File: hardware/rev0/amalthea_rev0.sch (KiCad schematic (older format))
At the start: 27 parts, among them J1 USB_B_Micro, J2 USB_B_Micro, J3 Conn_Coaxial, J4 Conn_Coaxial, J8 Conn_Coaxial, J9 Conn_Coaxial, SW1 BTN_RECOVERY, SW2 BTN_DFU, SW3 BTN_RESET, Y1 DSC60xx

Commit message: Pick part numbers for BOM
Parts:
- D1, D8: Manufacturer_Part_Number (none) -> PMEG3050EP,115
- D2: Manufacturer_Part_Number (none) -> KR DELMS1.22-RHSI-24-E6L6
- D3: Manufacturer_Part_Number (none) -> KO DELMS1.22-SGTH-24-E6L6
- D4: Manufacturer_Part_Number (none) -> KY DELMS1.22-RHSI-26-G6N4
- D5: Manufacturer_Part_Number (none) -> KG DELMS1.22-PHQI-24-E6L6
- D6: Manufacturer_Part_Number (none) -> KB DELPS2.12-QHRI-24-Z555-10-S
- J1, J2: Manufacturer_Part_Number (none) -> 10103594-0001LF
- J3, J4, J8, J9: Manufacturer_Part_Number (none) -> CONSMA003.062
- R26, R27, R28, R29, R30, R31: Manufacturer_Part_Number (none) -> CRCW0402330RFKEDC
- SW1, SW2, SW3: Manufacturer_Part_Number (none) -> FSMRA3JH
- Y1: Manufacturer_Part_Number (none) -> DSC6001MI2A-060.0000
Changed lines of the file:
@@
 F 2 "amalthea:SOD128" H 6300 4850 50  0001 C CNN
 F 3 "~" H 6300 4850 50  0001 C CNN
+F 4 "PMEG3050EP,115" H 6300 4850 50  0001 C CNN "Manufacturer_Part_Number"
 	1    6300 4850
 	1    0    0    -1
@@
 F 2 "Connector_USB:USB_Micro-B_Amphenol_10103594-0001LF_Horizontal" H 7250 5000 50  0001 C CNN
 F 3 "~" H 7250 5000 50  0001 C CNN
+F 4 "10103594-0001LF" H 7100 5050 50  0001 C CNN "Manufacturer_Part_Number"
 	1    7100 5050
 	-1   0    0    -1
@@
 F 2 "Connector_USB:USB_Micro-B_Amphenol_10103594-0001LF_Horizontal" H 1050 3850 50  0001 C CNN
 F 3 "~" H 1050 3850 50  0001 C CNN
+F 4 "10103594-0001LF" H 900 3900 50  0001 C CNN "Manufacturer_Part_Number"
 	1    900  3900
 	1    0    0    -1
@@
 F 2 "amalthea:SOD128" H 1350 3550 50  0001 C CNN
 F 3 "~" H 1350 3550 50  0001 C CNN
+F 4 "PMEG3050EP,115" H 1350 3550 50  0001 C CNN "Manufacturer_Part_Number"
 	1    1350 3550
 	-1   0    0    1
@@
 F 2 "Crystal:Crystal_SMD_2016-4Pin_2.0x1.6mm" H 1050 2400 50  0001 C CNN
 F 3 "" H 1050 2400 50  0001 C CNN
+F 4 "DSC6001MI2A-060.0000 " H 1050 2400 50  0001 C CNN "Manufacturer_Part_Number"
 	1    1050 2400
 	1    0    0    -1
@@
 F 2 "amalthea:SWITCH-FSMRA" H 2250 5350 50  0001 C CNN
 F 3 "~" H 2250 5350 50  0001 C CNN
+F 4 "FSMRA3JH" H 2250 5350 50  0001 C CNN "Manufacturer_Part_Number"
 	1    2250 5350
 	1    0    0    -1
@@
 F 2 "amalthea:SWITCH-FSMRA" H 2250 5650 50  0001 C CNN
 F 3 "~" H 2250 5650 50  0001 C CNN
+F 4 "FSMRA3JH" H 2250 5650 50  0001 C CNN "Manufacturer_Part_Number"
 	1    2250 5650
 	1    0    0    -1
@@
 F 2 "amalthea:SWITCH-FSMRA" H 2250 6000 50  0001 C CNN
 F 3 "~" H 2250 6000 50  0001 C CNN
+F 4 "FSMRA3JH" H 2250 6000 50  0001 C CNN "Manufacturer_Part_Number"
 	1    2250 6000
 	1    0    0    -1
@@
 F 2 "Resistor_SMD:R_0402_1005Metric" V 9380 4900 50  0001 C CNN
 F 3 "~" H 9450 4900 50  0001 C CNN
+F 4 "CRCW0402330RFKEDC" H 9450 4900 50  0001 C CNN "Manufacturer_Part_Number"
 	1    9450 4900
 	0    1    1    0
@@
 F 2 "Resistor_SMD:R_0402_1005Metric" V 9380 5000 50  0001 C CNN
 F 3 "~" H 9450 5000 50  0001 C CNN
+F 4 "CRCW0402330RFKEDC" H 9450 5000 50  0001 C CNN "Manufacturer_Part_Number"
 	1    9450 5000
 	0    1    1    0
@@
 F 2 "Resistor_SMD:R_0402_1005Metric" V 9380 5100 50  0001 C CNN
 F 3 "~" H 9450 5100 50  0001 C CNN
+F 4 "CRCW0402330RFKEDC" H 9450 5100 50  0001 C CNN "Manufacturer_Part_Number"
 	1    9450 5100
 	0    1    1    0
@@
 F 2 "Resistor_SMD:R_0402_1005Metric" V 9380 5200 50  0001 C CNN
 F 3 "~" H 9450 5200 50  0001 C CNN
+F 4 "CRCW0402330RFKEDC" H 9450 5200 50  0001 C CNN "Manufacturer_Part_Number"
 	1    9450 5200
 	0    1    1    0
@@
 F 2 "Resistor_SMD:R_0402_1005Metric" V 9380 5300 50  0001 C CNN
 F 3 "~" H 9450 5300 50  0001 C CNN
+F 4 "CRCW0402330RFKEDC" H 9450 5300 50  0001 C CNN "Manufacturer_Part_Number"
 	1    9450 5300
 	0    1    1    0
@@
 F 2 "Resistor_SMD:R_0402_1005Metric" V 9380 5400 50  0001 C CNN
 F 3 "~" H 9450 5400 50  0001 C CNN
+F 4 "CRCW0402330RFKEDC" H 9450 5400 50  0001 C CNN "Manufacturer_Part_Number"
 	1    9450 5400
 	0    1    1    0
@@
 F 2 "LED_SMD:LED_0603_1608Metric_Pad1.05x0.95mm_HandSolder" H 9950 4900 50  0001 C CNN
 F 3 "~" H 9950 4900 50  0001 C CNN
+F 4 "KR DELMS1.22-RHSI-24-E6L6" H 9950 4900 50  0001 C CNN "Manufacturer_Part_Number"
 	1    9950 4900
 	1    0    0    -1
@@
 F 2 "LED_SMD:LED_0603_1608Metric_Pad1.05x0.95mm_HandSolder" H 9950 5100 50  0001 C CNN
 F 3 "~" H 9950 5100 50  0001 C CNN
+F 4 "KY DELMS1.22-RHSI-26-G6N4" H 9950 5100 50  0001 C CNN "Manufacturer_Part_Number"
 	1    9950 5100
 	1    0    0    -1
@@
 F 2 "LED_SMD:LED_0603_1608Metric_Pad1.05x0.95mm_HandSolder" H 9950 5200 50  0001 C CNN
 F 3 "~" H 9950 5200 50  0001 C CNN
+F 4 "KG DELMS1.22-PHQI-24-E6L6" H 9950 5200 50  0001 C CNN "Manufacturer_Part_Number"
 	1    9950 5200
 	1    0    0    -1
@@
 F 2 "LED_SMD:LED_0603_1608Metric_Pad1.05x0.95mm_HandSolder" H 9950 5300 50  0001 C CNN
 F 3 "~" H 9950 5300 50  0001 C CNN
+F 4 "KB DELPS2.12-QHRI-24-Z555-10-S" H 9950 5300 50  0001 C CNN "Manufacturer_Part_Number"
 	1    9950 5300
 	1    0    0    -1
@@
 F 2 "amalthea:SMA-EDGE" H 3700 4200 50  0001 C CNN
 F 3 " ~" H 3700 4200 50  0001 C CNN
+F 4 "CONSMA003.062" H 3700 4200 50  0001 C CNN "Manufacturer_Part_Number"
 	1    3700 4200
 	1    0    0    -1
@@
 F 2 "amalthea:SMA-EDGE" H 3700 3700 50  0001 C CNN
 F 3 " ~" H 3700 3700 50  0001 C CNN
+F 4 "CONSMA003.062" H 3700 3700 50  0001 C CNN "Manufacturer_Part_Number"
 	1    3700 3700
 	1    0    0    -1
@@
 F 2 "LED_SMD:LED_0603_1608Metric_Pad1.05x0.95mm_HandSolder" H 9950 5000 50  0001 C CNN
 F 3 "~" H 9950 5000 50  0001 C CNN
+F 4 "KO DELMS1.22-SGTH-24-E6L6" H 9950 5000 50  0001 C CNN "Manufacturer_Part_Number"
 	1    9950 5000
 	1    0    0    -1
@@
 F 2 "amalthea:SMA-EDGE" H 7100 3050 50  0001 C CNN
 F 3 " ~" H 7100 3050 50  0001 C CNN
+F 4 "CONSMA003.062" H 7100 3050 50  0001 C CNN "Manufacturer_Part_Number"
 	1    7100 3050
 	1    0    0    -1
@@
 F 2 "amalthea:SMA-EDGE" H 7100 3650 50  0001 C CNN
 F 3 " ~" H 7100 3650 50  0001 C CNN
+F 4 "CONSMA003.062" H 7100 3650 50  0001 C CNN "Manufacturer_Part_Number"
 	1    7100 3650
 	1    0    0    -1

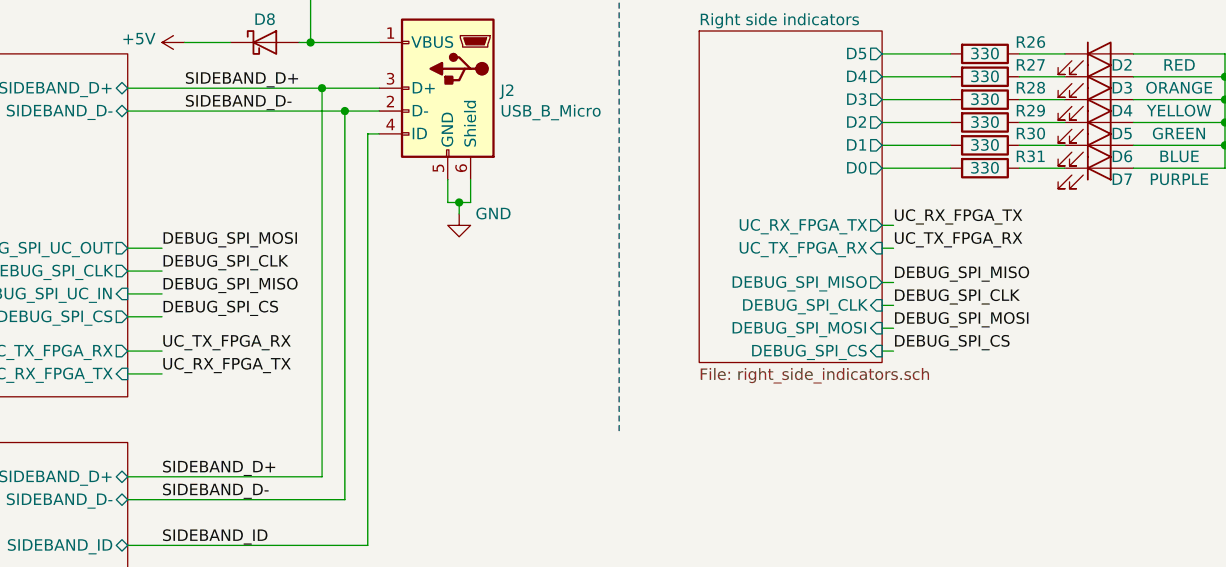
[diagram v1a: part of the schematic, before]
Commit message: hardware: adopt OSHWA convention for SPI signal names
https://www.oshwa.org/a-resolution-to-redefine-spi-signal-names
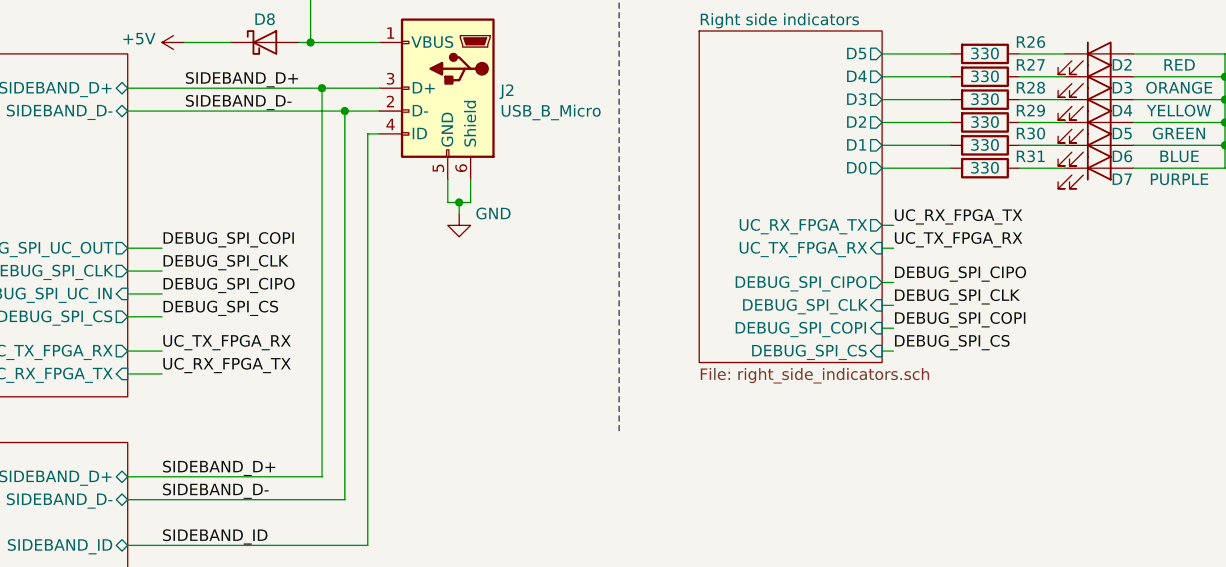
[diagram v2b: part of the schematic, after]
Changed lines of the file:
@@
 	5700 5750 5850 5750
 Text Label 5850 5750 0    50   ~ 0
-DEBUG_SPI_MOSI
+DEBUG_SPI_COPI
 Wire Wire Line
 	5700 5850 5850 5850
@@
 	5700 5950 5850 5950
 Text Label 5850 5950 0    50   ~ 0
-DEBUG_SPI_MISO
+DEBUG_SPI_CIPO
 Text Label 5850 5850 0    50   ~ 0
 DEBUG_SPI_CLK
@@
 $EndComp
 Text Label 9050 6100 0    50   ~ 0
-DEBUG_SPI_MOSI
+DEBUG_SPI_COPI
 $Comp
 L Device:R R26
@@
 F8 "UC_RX_FPGA_TX" O R 9000 5650 50
 F9 "UC_TX_FPGA_RX" I R 9000 5750 50
-F10 "DEBUG_SPI_MISO" O R 9000 5900 50
+F10 "DEBUG_SPI_CIPO" O R 9000 5900 50
 F11 "DEBUG_SPI_CLK" I R 9000 6000 50
-F12 "DEBUG_SPI_MOSI" I R 9000 6100 50
+F12 "DEBUG_SPI_COPI" I R 9000 6100 50
 F13 "DEBUG_SPI_CS" I R 9000 6200 50
 $EndSheet
@@
 DEBUG_SPI_CLK
 Text Label 9050 5900 0    50   ~ 0
-DEBUG_SPI_MISO
+DEBUG_SPI_CIPO
 Text Label 9050 6200 0    50   ~ 0
 DEBUG_SPI_CS
